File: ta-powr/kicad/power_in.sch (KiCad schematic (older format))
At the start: 14 parts, among them U1 SPV1040

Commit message: added footprint libraries
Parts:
- U1: footprint (none) -> Package_SO:TSSOP-8_4.4x3mm_P0.65mm
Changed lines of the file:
@@
 F 0 "U1" H 5775 4125 50  0000 C CNN
 F 1 "SPV1040" H 5775 4034 50  0000 C CNN
-F 2 "" H 5700 3650 50  0001 C CNN
+F 2 "Package_SO:TSSOP-8_4.4x3mm_P0.65mm" H 5700 3650 50  0001 C CNN
 F 3 "" H 5700 3650 50  0001 C CNN
 	1    5700 3550

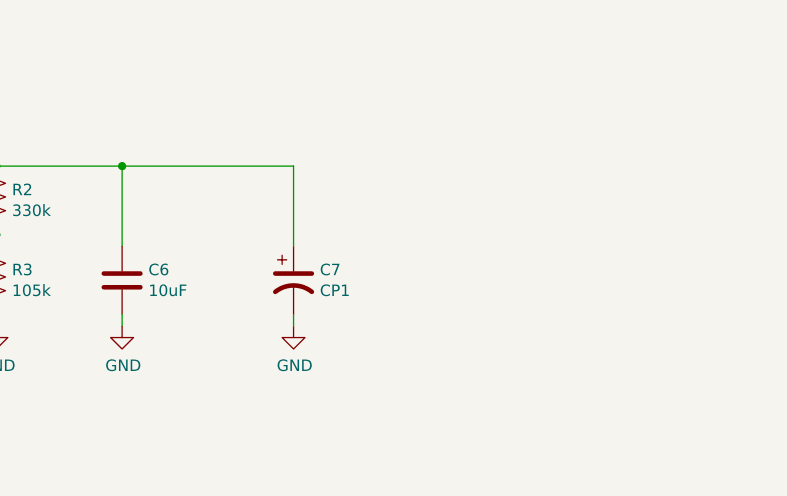
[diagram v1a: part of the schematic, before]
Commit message: added footprint for kemet cap
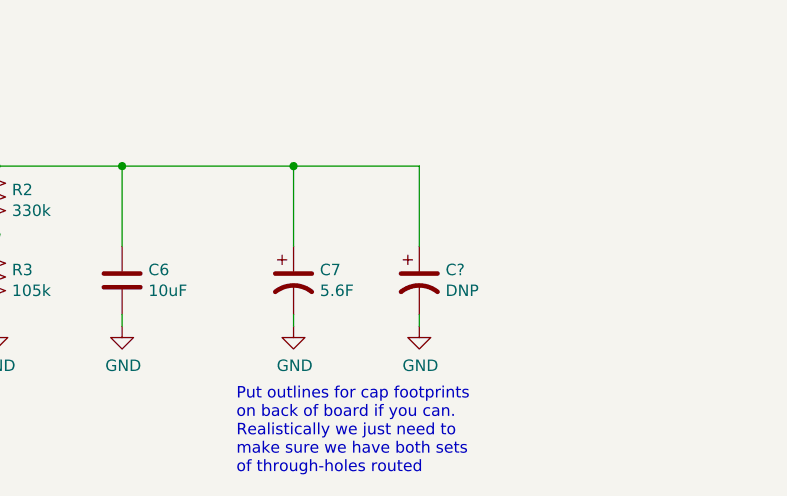
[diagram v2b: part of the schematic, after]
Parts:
- added C?: DNP, ta-powr:TECATE_PBL, symbol Device:CP1
- C7: value CP1 -> 5.6F; footprint (none) -> ta-powr:FT0H565ZF
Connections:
- wire segments 51 -> 54
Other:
- note added: "Put outlines for cap footprints \non back of board if you can. \nRealistically we just need to \nmake sure we have both sets\nof through-holes routed"
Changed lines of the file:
@@
 P 8400 4150
 F 0 "C7" H 8515 4196 50  0000 L CNN
-F 1 "CP1" H 8515 4105 50  0000 L CNN
-F 2 "" H 8400 4150 50  0001 C CNN
+F 1 "5.6F" H 8515 4105 50  0000 L CNN
+F 2 "ta-powr:FT0H565ZF" H 8400 4150 50  0001 C CNN
 F 3 "~" H 8400 4150 50  0001 C CNN
 	1    8400 4150
@@
 Wire Wire Line
 	3500 3200 3950 3200
+$Comp
+L Device:CP1 C?
+U 1 1 5F06D9D0
+P 8950 4150
+F 0 "C?" H 9065 4196 50  0000 L CNN
+F 1 "DNP" H 9065 4105 50  0000 L CNN
+F 2 "ta-powr:TECATE_PBL" H 8950 4150 50  0001 C CNN
+F 3 "~" H 8950 4150 50  0001 C CNN
+	1    8950 4150
+	1    0    0    -1
+$EndComp
+Wire Wire Line
+	8950 3650 8950 4000
+$Comp
+L power:GND #PWR?
+U 1 1 5F06D9D7
+P 8950 4350
+F 0 "#PWR?" H 8950 4100 50  0001 C CNN
+F 1 "GND" H 8955 4177 50  0000 C CNN
+F 2 "" H 8950 4350 50  0001 C CNN
+F 3 "" H 8950 4350 50  0001 C CNN
+	1    8950 4350
+	1    0    0    -1
+$EndComp
+Wire Wire Line
+	8950 4300 8950 4350
+Wire Wire Line
+	8400 3650 8950 3650
+Connection ~ 8400 3650
+Text Notes 8150 5000 0    50   ~ 0
+Put outlines for cap footprints \non back of board if you can. \nRealistically we just need to \nmake sure we have both sets\nof through-holes routed
 $EndSCHEMATC

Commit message: Added parts that are likely a problem
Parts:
- removed D2: 5.4V, symbol Device:D_Zener
- added C17: 1uF, symbol Device:C
- added D2: D_Zener_AKA, Package_TO_SOT_SMD:SOT-89-3, symbol power-board:D_Zener_AKA
- added R19, R20: 1, Resistor_SMD:R_2512_6332Metric, symbol Device:R_US
- added R21, R23, R25, R27: 4M, symbol Device:R_US
- added R22, R24, R26, R28: 6M, symbol Device:R_US
- added U3: TLV8544DT, D14_TEX, symbol power-board:TLV8544DT
- added U4: ADS1115-Q1, Package_SO:TSSOP-10_3x3mm_P0.5mm, symbol power-board:ADS1115-Q1
- D1: footprint (none) -> Diode_SMD:D_SOD-123F; Manufacturer Part Number (none) -> NRVB120VLSFT1G; Vendor (none) -> Digikey; Vendor Part Number (none) -> NRVB120VLSFT1GOSCT-ND
- L1: footprint (none) -> ta-powr:IHLP-2525CZ-8A; Manufacturer Part Number (none) -> IHLP2525CZER150M8A; Vendor (none) -> Digikey; Vendor Part Number (none) -> 541-2173-1-ND
- gave numbers to parts that had none: 1
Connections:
- net labels added: ADC_ALERT, SCL, SDA, V_cap, V_cap+, V_cap-, V_cap_meas, V_harv, V_harv_meas, V_out_meas, V_sol+, V_sol-, V_solar, V_solar_meas, Vdd_IN, Vdd_IN_loc
- wire segments 54 -> 113
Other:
- note added: "Attach the IN+ pins to their respective\nnets as close as possible to the shunt\nresistor."
- moved on the sheet: C1, C18, C2, C3, C4, C5, C6, C7, D1, L1, R1, R2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

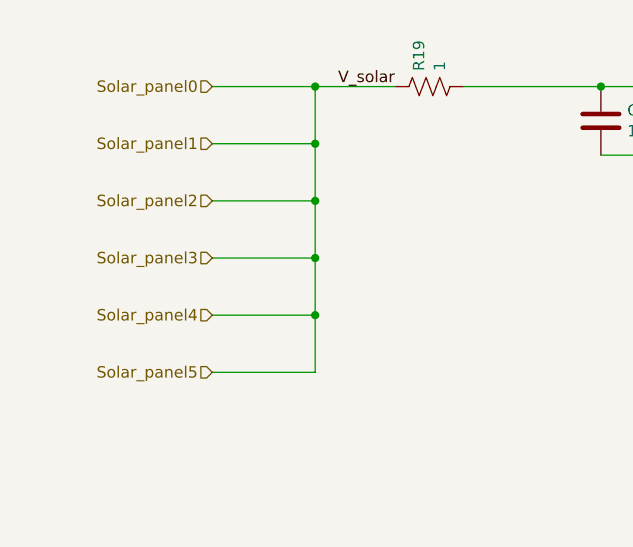
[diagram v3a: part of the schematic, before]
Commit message: added header schematic connections, added footprints to effectively every part, still need to check for bugs
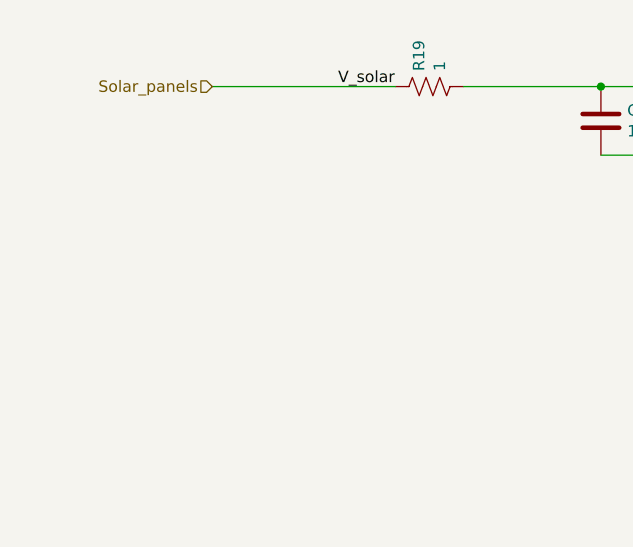
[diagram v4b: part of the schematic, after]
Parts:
- C1, C17, C2, C3, C4, C5, C6: footprint (none) -> Capacitor_SMD:C_0603_1608Metric
- R1, R2, R21, R22, R23, R24, R25, R26, R27, R28, R3: footprint (none) -> Resistor_SMD:R_0603_1608Metric
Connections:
- net labels added: Solar_panels
- net labels removed: Solar_panel0, Solar_panel1, Solar_panel2, Solar_panel3, Solar_panel4, Solar_panel5
- wire segments 113 -> 102
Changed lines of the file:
@@
 $Descr A4 11693 8268
 encoding utf-8
-Sheet 2 3
+Sheet 3 3
 Title "Input Booster and Cap"
 Date "2020-06-22"
@@
 $EndDescr
 Text HLabel 1550 1550 0    50   Input ~ 0
-Solar_panel0
-Text HLabel 1550 1800 0    50   Input ~ 0
-Solar_panel1
-Text HLabel 1550 2050 0    50   Input ~ 0
-Solar_panel2
-Text HLabel 1550 2300 0    50   Input ~ 0
-Solar_panel3
-Text HLabel 1550 2550 0    50   Input ~ 0
-Solar_panel4
-Text HLabel 1550 2800 0    50   Input ~ 0
-Solar_panel5
+Solar_panels
 Text HLabel 9900 2000 2    50   Output ~ 0
 Vcap
-Wire Wire Line
-	2000 1550 2000 1800
-Wire Wire Line
-	2000 2800 1550 2800
-Wire Wire Line
-	1550 2550 2000 2550
-Connection ~ 2000 2550
-Wire Wire Line
-	2000 2550 2000 2800
-Wire Wire Line
-	1550 2300 2000 2300
-Connection ~ 2000 2300
-Wire Wire Line
-	2000 2300 2000 2550
-Wire Wire Line
-	1550 2050 2000 2050
-Connection ~ 2000 2050
-Wire Wire Line
-	2000 2050 2000 2300
-Wire Wire Line
-	1550 1800 2000 1800
-Connection ~ 2000 1800
-Wire Wire Line
-	2000 1800 2000 2050
-Connection ~ 2000 1550
-Wire Wire Line
-	1550 1550 2000 1550
 Wire Wire Line
 	3500 1850 3500 2050
@@
 F 0 "C2" H 3815 1746 50  0000 L CNN
 F 1 "10uF" H 3815 1655 50  0000 L CNN
-F 2 "" H 3738 1550 50  0001 C CNN
+F 2 "Capacitor_SMD:C_0603_1608Metric" H 3738 1550 50  0001 C CNN
 F 3 "~" H 3700 1700 50  0001 C CNN
 F 4 "" H 3700 1700 50  0001 C CNN "Vendor part number"
@@
 F 0 "C1" H 3365 1746 50  0000 L CNN
 F 1 "10uF" H 3365 1655 50  0000 L CNN
-F 2 "" H 3288 1550 50  0001 C CNN
+F 2 "Capacitor_SMD:C_0603_1608Metric" H 3288 1550 50  0001 C CNN
 F 3 "~" H 3250 1700 50  0001 C CNN
-F 4 "" H 3250 1700 50  0001 C CNN "Manufacturer Part Number"
-F 5 "" H 3250 1700 50  0001 C CNN "Vendor part number"
-F 6 "" H 3250 1700 50  0001 C CNN "Vendor"
+F 4 "" H 3250 1700 50  0001 C CNN "Vendor part number"
 	1    3250 1700
 	1    0    0    -1
@@
 F 0 "C3" H 4765 1746 50  0000 L CNN
 F 1 "100nF" H 4765 1655 50  0000 L CNN
-F 2 "" H 4688 1550 50  0001 C CNN
+F 2 "Capacitor_SMD:C_0603_1608Metric" H 4688 1550 50  0001 C CNN
 F 3 "~" H 4650 1700 50  0001 C CNN
 F 4 "" H 4650 1700 50  0001 C CNN "Vendor part number"
@@
 F 0 "C4" H 5015 2496 50  0000 L CNN
 F 1 "4.7uF" H 5015 2405 50  0000 L CNN
-F 2 "" H 4938 2300 50  0001 C CNN
+F 2 "Capacitor_SMD:C_0603_1608Metric" H 4938 2300 50  0001 C CNN
 F 3 "~" H 4900 2450 50  0001 C CNN
 F 4 "" H 4900 2450 50  0001 C CNN "Vendor part number"
@@
 F 0 "C5" H 6265 2496 50  0000 L CNN
 F 1 "1nF" H 6265 2405 50  0000 L CNN
-F 2 "" H 6188 2300 50  0001 C CNN
+F 2 "Capacitor_SMD:C_0603_1608Metric" H 6188 2300 50  0001 C CNN
 F 3 "~" H 6150 2450 50  0001 C CNN
 F 4 "" H 6150 2450 50  0001 C CNN "Vendor part number"
@@
 F 0 "R1" H 4168 1746 50  0000 L CNN
 F 1 "1k" H 4168 1655 50  0000 L CNN
-F 2 "" V 4140 1690 50  0001 C CNN
+F 2 "Resistor_SMD:R_0603_1608Metric" V 4140 1690 50  0001 C CNN
 F 3 "~" H 4100 1700 50  0001 C CNN
 	1    4100 1700
@@
 F 0 "R2" H 6918 2196 50  0000 L CNN
 F 1 "330k" H 6918 2105 50  0000 L CNN
-F 2 "" V 6890 2140 50  0001 C CNN
+F 2 "Resistor_SMD:R_0603_1608Metric" V 6890 2140 50  0001 C CNN
 F 3 "~" H 6850 2150 50  0001 C CNN
 	1    6850 2150
@@
 F 0 "R3" H 6918 2546 50  0000 L CNN
 F 1 "105k" H 6918 2455 50  0000 L CNN
-F 2 "" V 6890 2490 50  0001 C CNN
+F 2 "Resistor_SMD:R_0603_1608Metric" V 6890 2490 50  0001 C CNN
 F 3 "~" H 6850 2500 50  0001 C CNN
 	1    6850 2500
@@
 F 0 "C6" H 7515 2546 50  0000 L CNN
 F 1 "10uF" H 7515 2455 50  0000 L CNN
-F 2 "" H 7438 2350 50  0001 C CNN
+F 2 "Capacitor_SMD:C_0603_1608Metric" H 7438 2350 50  0001 C CNN
 F 3 "~" H 7400 2500 50  0001 C CNN
 F 4 "" H 7400 2500 50  0001 C CNN "Vendor part number"
@@
 	0    -1   -1   0
 $EndComp
-Wire Wire Line
-	2000 1550 2350 1550
 Text Label 2100 1550 0    50   ~ 0
 V_solar
@@
 F 0 "C17" H 4465 6146 50  0000 L CNN
 F 1 "1uF" H 4465 6055 50  0000 L CNN
-F 2 "" H 4388 5950 50  0001 C CNN
+F 2 "Capacitor_SMD:C_0603_1608Metric" H 4388 5950 50  0001 C CNN
 F 3 "~" H 4350 6100 50  0001 C CNN
 F 4 "" H 4350 6100 50  0001 C CNN "Vendor part number"
@@
 F 0 "R21" H 1018 4046 50  0000 L CNN
 F 1 "4M" H 1018 3955 50  0000 L CNN
-F 2 "" V 990 3990 50  0001 C CNN
+F 2 "Resistor_SMD:R_0603_1608Metric" V 990 3990 50  0001 C CNN
 F 3 "~" H 950 4000 50  0001 C CNN
 	1    950  4000
@@
 F 0 "R22" H 1018 4546 50  0000 L CNN
 F 1 "6M" H 1018 4455 50  0000 L CNN
-F 2 "" V 990 4490 50  0001 C CNN
+F 2 "Resistor_SMD:R_0603_1608Metric" V 990 4490 50  0001 C CNN
 F 3 "~" H 950 4500 50  0001 C CNN
 	1    950  4500
@@
 F 0 "R23" H 1718 4046 50  0000 L CNN
 F 1 "4M" H 1718 3955 50  0000 L CNN
-F 2 "" V 1690 3990 50  0001 C CNN
+F 2 "Resistor_SMD:R_0603_1608Metric" V 1690 3990 50  0001 C CNN
 F 3 "~" H 1650 4000 50  0001 C CNN
 	1    1650 4000
@@
 F 0 "R24" H 1718 4546 50  0000 L CNN
 F 1 "6M" H 1718 4455 50  0000 L CNN
-F 2 "" V 1690 4490 50  0001 C CNN
+F 2 "Resistor_SMD:R_0603_1608Metric" V 1690 4490 50  0001 C CNN
 F 3 "~" H 1650 4500 50  0001 C CNN
 	1    1650 4500
@@
 F 0 "R27" H 2918 4046 50  0000 L CNN
 F 1 "4M" H 2918 3955 50  0000 L CNN
-F 2 "" V 2890 3990 50  0001 C CNN
+F 2 "Resistor_SMD:R_0603_1608Metric" V 2890 3990 50  0001 C CNN
 F 3 "~" H 2850 4000 50  0001 C CNN
 	1    2850 4000
@@
 F 0 "R28" H 2918 4546 50  0000 L CNN
 F 1 "6M" H 2918 4455 50  0000 L CNN
-F 2 "" V 2890 4490 50  0001 C CNN
+F 2 "Resistor_SMD:R_0603_1608Metric" V 2890 4490 50  0001 C CNN
 F 3 "~" H 2850 4500 50  0001 C CNN
 	1    2850 4500
@@
 F 0 "R25" H 2318 4046 50  0000 L CNN
 F 1 "4M" H 2318 3955 50  0000 L CNN
-F 2 "" V 2290 3990 50  0001 C CNN
+F 2 "Resistor_SMD:R_0603_1608Metric" V 2290 3990 50  0001 C CNN
 F 3 "~" H 2250 4000 50  0001 C CNN
 	1    2250 4000
@@
 F 0 "R26" H 2318 4546 50  0000 L CNN
 F 1 "6M" H 2318 4455 50  0000 L CNN
-F 2 "" V 2290 4490 50  0001 C CNN
+F 2 "Resistor_SMD:R_0603_1608Metric" V 2290 4490 50  0001 C CNN
 F 3 "~" H 2250 4500 50  0001 C CNN
 	1    2250 4500
@@
 	0    -1   -1   0
 $EndComp
+Wire Wire Line
+	1550 1550 2350 1550
 $EndSCHEMATC

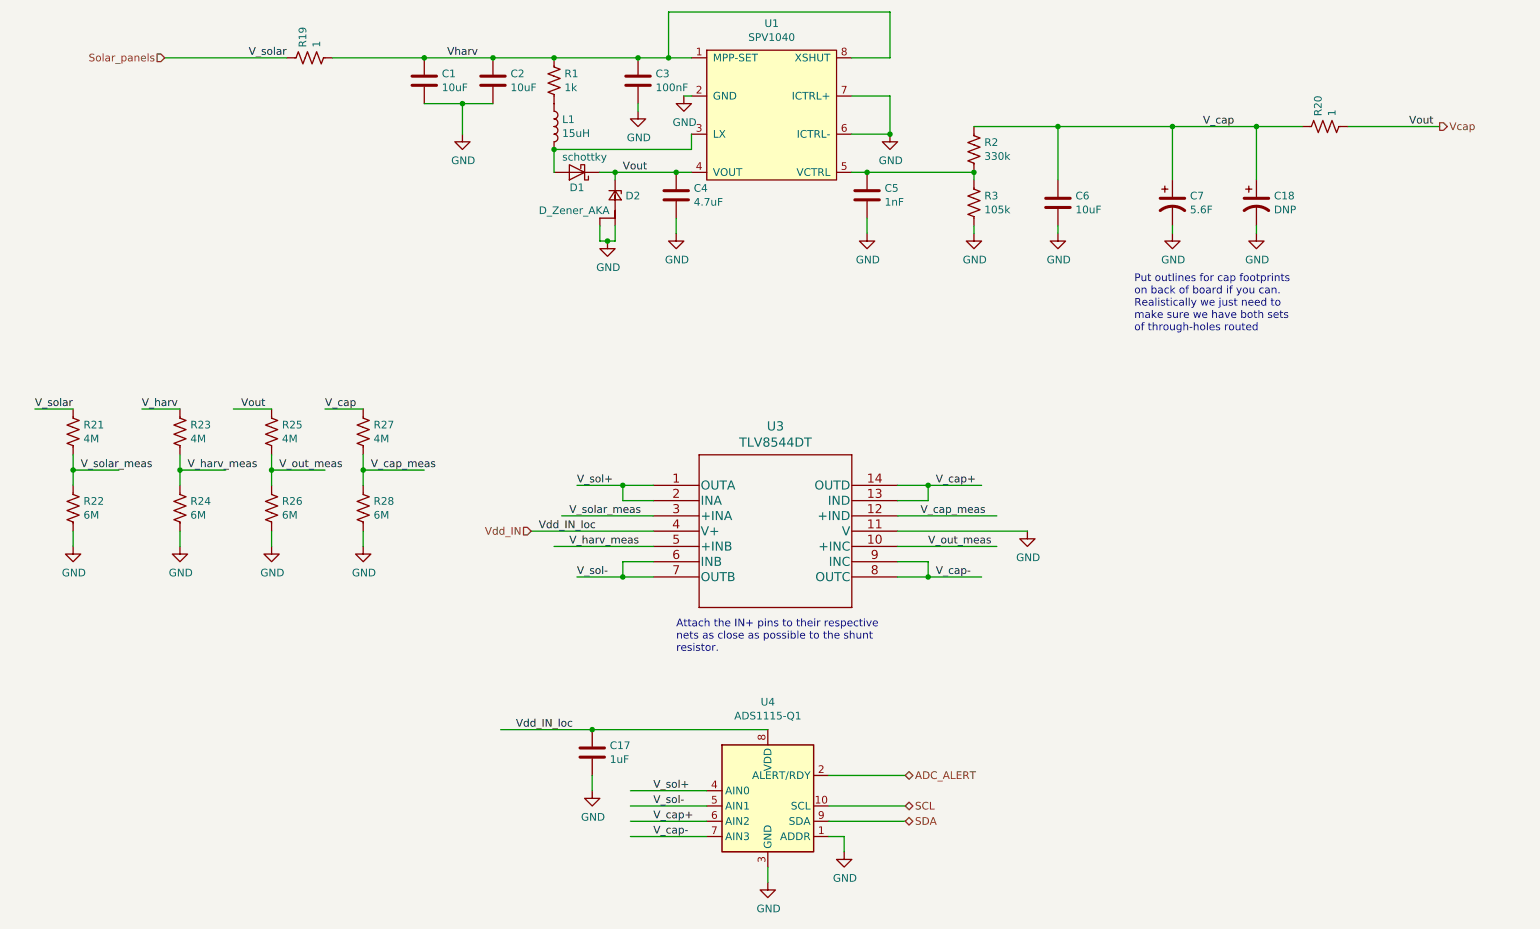
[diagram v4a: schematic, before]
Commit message: fixed electrical checker errors and generated netlist
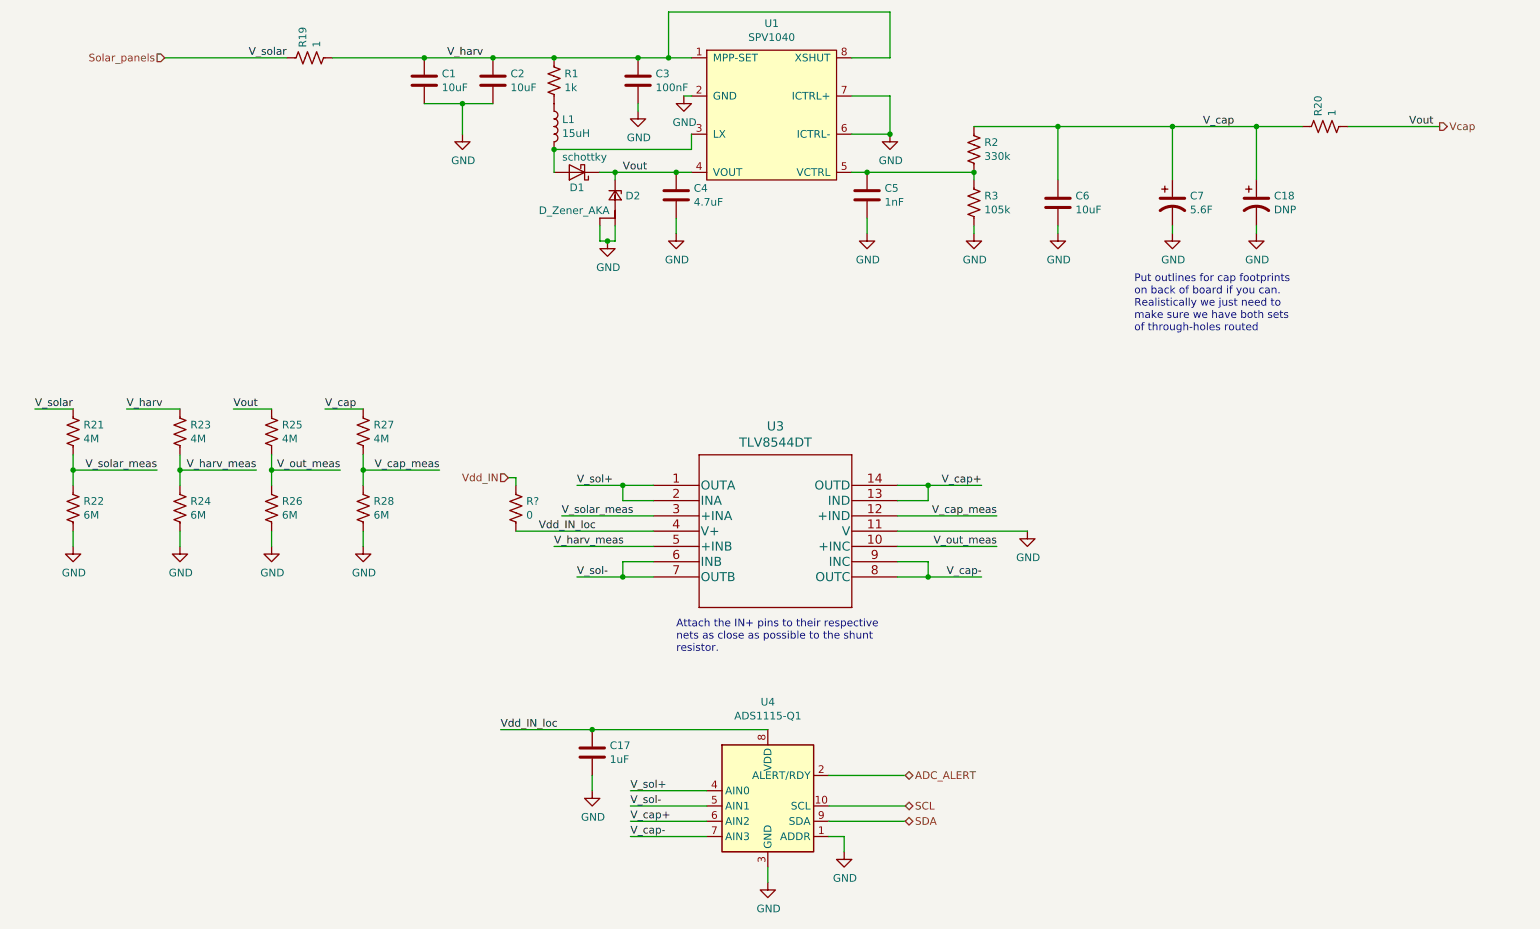
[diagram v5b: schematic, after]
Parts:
- added R?: 0, Resistor_SMD:R_0603_1608Metric, symbol Device:R_US
- U3: footprint D14_TEX -> ta-powr:TLV8544DT
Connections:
- net labels removed: Vharv
- wire segments 102 -> 104
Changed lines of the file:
@@
 Connection ~ 3700 1550
 Text Label 3400 1550 0    50   ~ 0
-Vharv
+V_harv
 Wire Wire Line
 	4850 1550 4850 1250
@@
 F 0 "U3" H 5550 4737 60  0000 C CNN
 F 1 "TLV8544DT" H 5550 4631 60  0000 C CNN
-F 2 "D14_TEX" H 5800 3600 60  0001 C CNN
+F 2 "ta-powr:TLV8544DT" H 5800 3600 60  0001 C CNN
 F 3 "" H 4750 4350 60  0000 C CNN
 	1    4750 4350
@@
 	1    0    0    -1
 $EndComp
-Text HLabel 3950 4650 0    50   Input ~ 0
+Text HLabel 3800 4300 0    50   Input ~ 0
 Vdd_IN
 Wire Wire Line
@@
 Wire Wire Line
 	4550 4850 4550 4950
-Wire Wire Line
-	4550 4950 4750 4950
-Text Label 1400 3850 0    50   ~ 0
+Text Label 1300 3850 0    50   ~ 0
 V_harv
 Wire Wire Line
@@
 Text Label 2600 3850 0    50   ~ 0
 V_cap
-Text Label 2050 3850 0    50   ~ 0
+Text Label 2000 3850 0    50   ~ 0
 Vout
 Text Notes 4900 5450 0    50   ~ 0
@@
 Wire Wire Line
 	5500 6850 5500 6950
-Wire Wire Line
-	4600 6350 5100 6350
-Text Label 4750 6350 0    50   ~ 0
+Text Label 4600 6350 0    50   ~ 0
 V_sol+
 Wire Wire Line
 	5100 6450 4600 6450
-Text Label 4750 6450 0    50   ~ 0
+Text Label 4600 6450 0    50   ~ 0
 V_sol-
 Wire Wire Line
@@
 Wire Wire Line
 	5100 6650 4600 6650
-Text Label 4750 6550 0    50   ~ 0
+Text Label 4600 6550 0    50   ~ 0
 V_cap+
-Text Label 4750 6650 0    50   ~ 0
+Text Label 4600 6650 0    50   ~ 0
 V_cap-
 Connection ~ 6550 4950
-Text Label 6600 4950 0    50   ~ 0
+Text Label 6900 4950 2    50   ~ 0
 V_cap-
 Connection ~ 6550 4350
-Text Label 6600 4350 0    50   ~ 0
+Text Label 6900 4350 2    50   ~ 0
 V_cap+
 Connection ~ 4550 4350
 Text Label 4250 4350 0    50   ~ 0
 V_sol+
-Connection ~ 4550 4950
 Text Label 4250 4950 0    50   ~ 0
 V_sol-
@@
 Wire Wire Line
 	3750 5950 4350 5950
-Text Label 3850 5950 0    50   ~ 0
+Text Label 3750 5950 0    50   ~ 0
 Vdd_IN_loc
 Wire Wire Line
@@
 	1650 4650 1650 4750
 Wire Wire Line
-	1400 3850 1650 3850
-Wire Wire Line
 	4100 4750 4750 4750
 Wire Wire Line
@@
 $EndComp
 Wire Wire Line
-	2850 4650 2850 4750
-Wire Wire Line
 	2600 3850 2850 3850
 Wire Wire Line
@@
 Text Label 4000 4650 0    50   ~ 0
 Vdd_IN_loc
-Wire Wire Line
-	3950 4650 4750 4650
 Connection ~ 2850 4250
 Wire Wire Line
 	2850 4250 2850 4350
-Text Label 2900 4250 0    50   ~ 0
+Text Label 3350 4250 2    50   ~ 0
 V_cap_meas
-Text Label 2300 4250 0    50   ~ 0
+Text Label 2700 4250 2    50   ~ 0
 V_out_meas
 Wire Wire Line
@@
 Wire Wire Line
 	2250 4250 2250 4350
-Wire Wire Line
-	2250 4250 2600 4250
-Wire Wire Line
-	2850 4250 3250 4250
-Wire Wire Line
-	1650 4250 1950 4250
 Connection ~ 1650 4250
 Wire Wire Line
 	1650 4250 1650 4350
-Wire Wire Line
-	950  4250 1250 4250
 Connection ~ 950  4250
 Wire Wire Line
 	950  4250 950  4350
-Text Label 1700 4250 0    50   ~ 0
+Text Label 2150 4250 2    50   ~ 0
 V_harv_meas
-Text Label 1000 4250 0    50   ~ 0
+Text Label 1500 4250 2    50   ~ 0
 V_solar_meas
-Text Label 4200 4550 0    50   ~ 0
+Text Label 4150 4550 0    50   ~ 0
 V_solar_meas
-Text Label 4200 4750 0    50   ~ 0
+Text Label 4100 4750 0    50   ~ 0
 V_harv_meas
-Text Label 6500 4550 0    50   ~ 0
+Text Label 7000 4550 2    50   ~ 0
 V_cap_meas
 Wire Wire Line
@@
 Wire Wire Line
 	6350 4750 7000 4750
-Text Label 6550 4750 0    50   ~ 0
+Text Label 7000 4750 2    50   ~ 0
 V_out_meas
 Wire Wire Line
@@
 Wire Wire Line
 	1550 1550 2350 1550
+Wire Wire Line
+	2250 4250 2700 4250
+Wire Wire Line
+	2850 4250 3350 4250
+Wire Wire Line
+	950  4250 1500 4250
+Wire Wire Line
+	1650 4250 2150 4250
+Wire Wire Line
+	5100 6350 4600 6350
+Wire Wire Line
+	4750 4950 4550 4950
+Connection ~ 4550 4950
+Wire Wire Line
+	1300 3850 1650 3850
+Wire Wire Line
+	2850 4650 2850 4750
+$Comp
+L Device:R_US R?
+U 1 1 5F183712
+P 3850 4500
+F 0 "R?" H 3918 4546 50  0000 L CNN
+F 1 "0" H 3918 4455 50  0000 L CNN
+F 2 "Resistor_SMD:R_0603_1608Metric" V 3890 4490 50  0001 C CNN
+F 3 "~" H 3850 4500 50  0001 C CNN
+	1    3850 4500
+	1    0    0    -1
+$EndComp
+Wire Wire Line
+	3800 4300 3850 4300
+Wire Wire Line
+	3850 4300 3850 4350
+Wire Wire Line
+	3850 4650 4750 4650
 $EndSCHEMATC
